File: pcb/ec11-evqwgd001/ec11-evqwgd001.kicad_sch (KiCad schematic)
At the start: 10 parts, among them J1001 Conn_01x01_Socket, J1007 Conn_01x01_Socket, J1013 Conn_01x01_Socket, SW1001 EVQWGD001, SW1002 RotaryEncoder

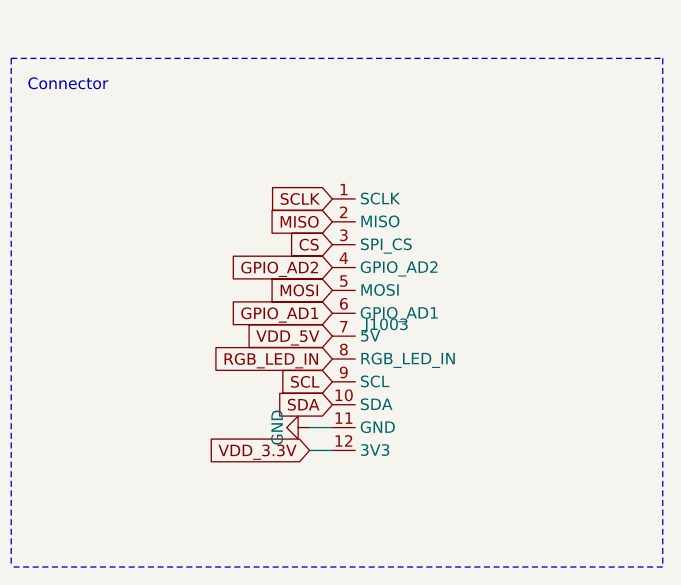
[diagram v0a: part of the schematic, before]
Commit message: updated vikm connector symbols, per some recommendations from sigprof in fingerpunch discord
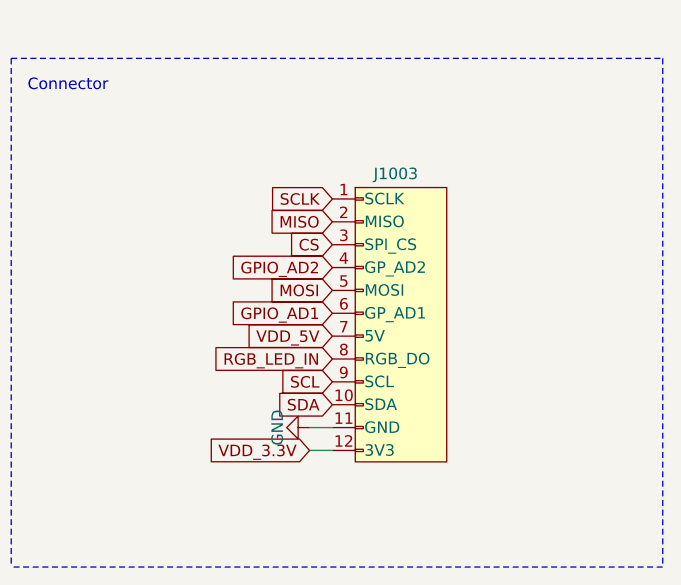
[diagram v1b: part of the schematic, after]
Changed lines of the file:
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@@
     )
   )
-  (symbol (lib_id "vik:vik-module-connector") (at 186.182 132.334 0) (unit 1)
-    (in_bom yes) (on_board yes) (dnp no) (fields_autoplaced)
-    (property "Reference" "J1003" (at 189.738 132.334 0)
+  (symbol (lib_id "vik:vik-module-connector") (at 193.802 131.064 0) (unit 1)
+    (in_bom yes) (on_board yes) (dnp no)
+    (property "Reference" "J1003" (at 190.754 115.57 0)
       (effects (font (size 1.27 1.27)) (justify left))
     )
-    (property "Value" "~" (at 186.182 125.984 0)
+    (property "Value" "~" (at 193.802 124.714 0)
       (effects (font (size 1.27 1.27)))
     )
-    (property "Footprint" "vik:vik-module-connector-horizontal" (at 186.182 125.984 0)
+    (property "Footprint" "vik:vik-module-connector-horizontal" (at 193.802 124.714 0)
       (effects (font (size 1.27 1.27)) hide)
     )
-    (property "Datasheet" "" (at 186.182 125.984 0)
+    (property "Datasheet" "" (at 193.802 124.714 0)
       (effects (font (size 1.27 1.27)) hide)
     )
-    (property "LCSC" "C2919557" (at 186.182 132.334 0)
+    (property "LCSC" "C2919557" (at 193.802 131.064 0)
       (effects (font (size 1.27 1.27)) hide)
     )

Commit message: incorrect copyright messages in some of the schema files
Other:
- company: bastard keyboards -> (none)
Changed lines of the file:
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@@
   (paper "A4")
   (title_block
-    (company "bastard keyboards")
-    (comment 4 "Copyright Quentin Lebastard")
+    (comment 4 "https://github.com/sadekbaroudi/vik")
   )
   (junction (at 125.476 53.086) (diameter 0) (color 0 0 0 0)
